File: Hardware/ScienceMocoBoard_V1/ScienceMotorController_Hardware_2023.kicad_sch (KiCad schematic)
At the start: 134 parts, among them Q1 SI4156DY, Q10 SI4156DY, Q11 SI4156DY, Q12 SI4156DY, Q13 SI4156DY, Q14 SI4156DY, Q15 SI4156DY, Q16 SI4156DY, Q2 SI4156DY, Q3 SI4156DY, Q4 SI4156DY, Q5 SI4156DY, Q6 SI4156DY, Q7 SI4156DY, Q8 SI4156DY, Q9 SI4156DY, U1 IRS2005S, U10 IRS2005S, U11 TM4C129E_Launchpad, U2 IRS2005S, U3 3V3 OKI, U4 TSR_1-2450, U5 IRS2005S, U6 IRS2005S, U7 IRS2005S, U8 IRS2005S, U9 IRS2005S

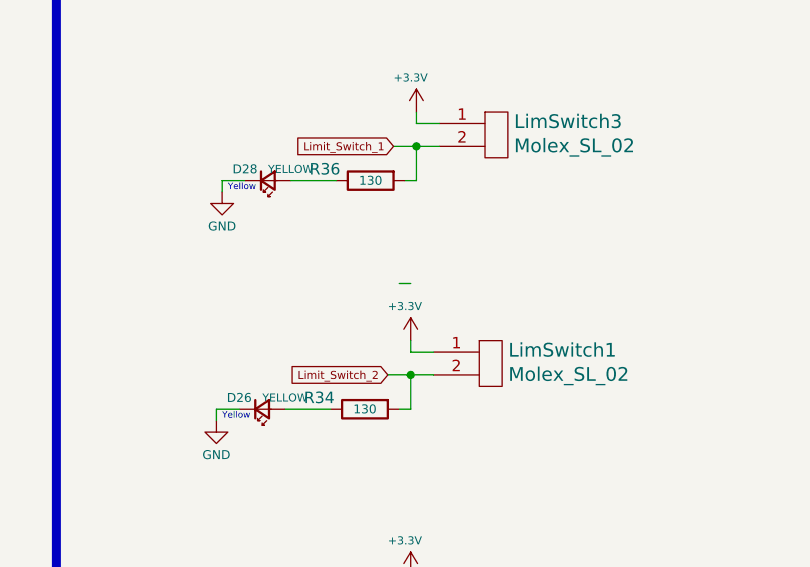
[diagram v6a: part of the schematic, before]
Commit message: Layout for Encoders, Servos, and Limit Switches
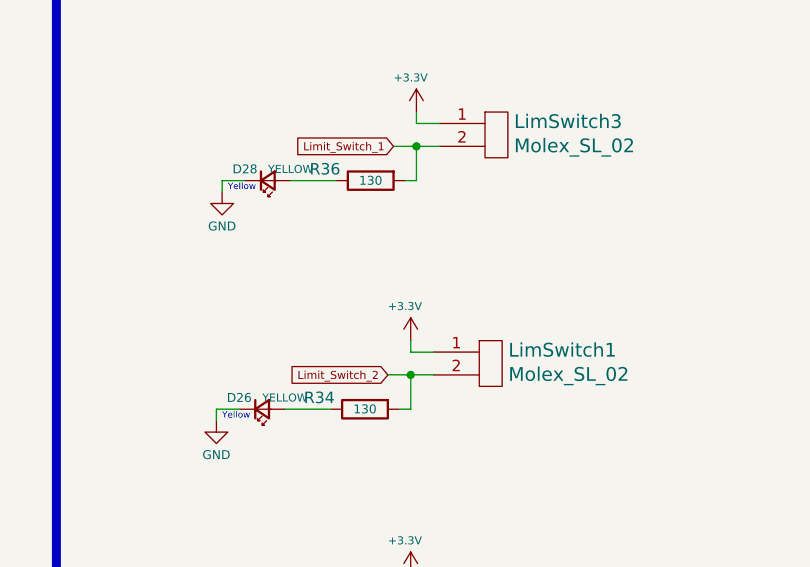
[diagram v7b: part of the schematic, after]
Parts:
- Conn1, Conn2, Conn3, Conn4, Conn5, Conn6, Conn7: footprint MRDT_Connectors:Square_Anderson_2_V_Side_By_Side -> MRDT_Connectors:Square_Anderson_2_H_Side_By_Side
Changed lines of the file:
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@@
     (stroke (width 0) (type default) (color 0 0 0 0))
   )
-  (wire (pts (xy 533.4 62.23) (xy 534.67 62.23))
-    (stroke (width 0) (type default) (color 0 0 0 0))
-  )
   (wire (pts (xy 364.49 105.41) (xy 377.19 105.41))
     (stroke (width 0) (type default) (color 0 0 0 0))
@@
       (effects (font (size 1.524 1.524)) (justify right))
     )
-    (property "Footprint" "MRDT_Connectors:Square_Anderson_2_V_Side_By_Side" (id 2) (at 52.07 330.835 0)
+    (property "Footprint" "MRDT_Connectors:Square_Anderson_2_H_Side_By_Side" (id 2) (at 52.07 330.835 0)
       (effects (font (size 1.524 1.524)) hide)
     )
@@
       (effects (font (size 1.524 1.524)) (justify right))
     )
-    (property "Footprint" "MRDT_Connectors:Square_Anderson_2_V_Side_By_Side" (id 2) (at 378.46 82.55 0)
+    (property "Footprint" "MRDT_Connectors:Square_Anderson_2_H_Side_By_Side" (id 2) (at 378.46 82.55 0)
       (effects (font (size 1.524 1.524)) hide)
     )
@@
       (effects (font (size 1.524 1.524)) (justify right))
     )
-    (property "Footprint" "MRDT_Connectors:Square_Anderson_2_V_Side_By_Side" (id 2) (at 377.825 168.91 0)
+    (property "Footprint" "MRDT_Connectors:Square_Anderson_2_H_Side_By_Side" (id 2) (at 377.825 168.91 0)
       (effects (font (size 1.524 1.524)) hide)
     )
@@
       (effects (font (size 1.524 1.524)))
     )
-    (property "Footprint" "MRDT_Connectors:Square_Anderson_2_V_Side_By_Side" (id 2) (at 139.7 201.93 0)
+    (property "Footprint" "MRDT_Connectors:Square_Anderson_2_H_Side_By_Side" (id 2) (at 139.7 201.93 0)
       (effects (font (size 1.524 1.524)) hide)
     )
@@
       (effects (font (size 1.524 1.524)) (justify right))
     )
-    (property "Footprint" "MRDT_Connectors:Square_Anderson_2_V_Side_By_Side" (id 2) (at 52.07 324.485 0)
+    (property "Footprint" "MRDT_Connectors:Square_Anderson_2_H_Side_By_Side" (id 2) (at 52.07 324.485 0)
       (effects (font (size 1.524 1.524)) hide)
     )
@@
       (effects (font (size 1.524 1.524)) (justify right))
     )
-    (property "Footprint" "MRDT_Connectors:Square_Anderson_2_V_Side_By_Side" (id 2) (at 137.16 168.91 0)
+    (property "Footprint" "MRDT_Connectors:Square_Anderson_2_H_Side_By_Side" (id 2) (at 137.16 168.91 0)
       (effects (font (size 1.524 1.524)) hide)
     )
@@
       (effects (font (size 1.524 1.524)))
     )
-    (property "Footprint" "MRDT_Connectors:Square_Anderson_2_V_Side_By_Side" (id 2) (at 380.365 201.93 0)
+    (property "Footprint" "MRDT_Connectors:Square_Anderson_2_H_Side_By_Side" (id 2) (at 380.365 201.93 0)
       (effects (font (size 1.524 1.524)) hide)
     )
@@
       (effects (font (size 1.524 1.524)) (justify right))
     )
-    (property "Footprint" "MRDT_Connectors:Square_Anderson_2_V_Side_By_Side" (id 2) (at 52.07 309.245 0)
+    (property "Footprint" "MRDT_Connectors:Square_Anderson_2_H_Side_By_Side" (id 2) (at 52.07 309.245 0)
       (effects (font (size 1.524 1.524)) hide)
     )
@@
       (effects (font (size 1.524 1.524)) (justify right))
     )
-    (property "Footprint" "MRDT_Connectors:Square_Anderson_2_V_Side_By_Side" (id 2) (at 133.35 82.55 0)
+    (property "Footprint" "MRDT_Connectors:Square_Anderson_2_H_Side_By_Side" (id 2) (at 133.35 82.55 0)
       (effects (font (size 1.524 1.524)) hide)
     )
@@
       (effects (font (size 1.524 1.524)))
     )
-    (property "Footprint" "MRDT_Connectors:Square_Anderson_2_V_Side_By_Side" (id 2) (at 27.94 321.945 0)
+    (property "Footprint" "MRDT_Connectors:Square_Anderson_2_H_Side_By_Side" (id 2) (at 27.94 321.945 0)
       (effects (font (size 1.524 1.524)) hide)
     )
@@
       (effects (font (size 1.524 1.524)) (justify right))
     )
-    (property "Footprint" "MRDT_Connectors:Square_Anderson_2_V_Side_By_Side" (id 2) (at 52.07 302.895 0)
+    (property "Footprint" "MRDT_Connectors:Square_Anderson_2_H_Side_By_Side" (id 2) (at 52.07 302.895 0)
       (effects (font (size 1.524 1.524)) hide)
     )
@@
       (effects (font (size 1.524 1.524)))
     )
-    (property "Footprint" "MRDT_Connectors:Square_Anderson_2_V_Side_By_Side" (id 2) (at 27.94 315.595 0)
+    (property "Footprint" "MRDT_Connectors:Square_Anderson_2_H_Side_By_Side" (id 2) (at 27.94 315.595 0)
       (effects (font (size 1.524 1.524)) hide)
     )
@@
       (effects (font (size 1.524 1.524)))
     )
-    (property "Footprint" "MRDT_Connectors:Square_Anderson_2_V_Side_By_Side" (id 2) (at 135.89 115.57 0)
+    (property "Footprint" "MRDT_Connectors:Square_Anderson_2_H_Side_By_Side" (id 2) (at 135.89 115.57 0)
       (effects (font (size 1.524 1.524)) hide)
     )
@@
       (effects (font (size 1.524 1.524)))
     )
-    (property "Footprint" "MRDT_Connectors:Square_Anderson_2_V_Side_By_Side" (id 2) (at 381 115.57 0)
+    (property "Footprint" "MRDT_Connectors:Square_Anderson_2_H_Side_By_Side" (id 2) (at 381 115.57 0)
       (effects (font (size 1.524 1.524)) hide)
     )
@@
     )
     (path "/b800eb0d-4e35-43a2-bf7a-748c18f9176e"
-      (reference "Conn1") (unit 1) (value "Input") (footprint "MRDT_Connectors:Square_Anderson_2_V_Side_By_Side")
+      (reference "Conn1") (unit 1) (value "Input") (footprint "MRDT_Connectors:Square_Anderson_2_H_Side_By_Side")
     )
     (path "/7ae2f7be-0b23-4959-82b9-533d8e3d95dd"
-      (reference "Conn1") (unit 2) (value "Input") (footprint "MRDT_Connectors:Square_Anderson_2_V_Side_By_Side")
+      (reference "Conn1") (unit 2) (value "Input") (footprint "MRDT_Connectors:Square_Anderson_2_H_Side_By_Side")
     )
     (path "/9c46e44a-301f-4adc-af9c-b892d007541c"
-      (reference "Conn2") (unit 1) (value "Output1") (footprint "MRDT_Connectors:Square_Anderson_2_V_Side_By_Side")
+      (reference "Conn2") (unit 1) (value "Output1") (footprint "MRDT_Connectors:Square_Anderson_2_H_Side_By_Side")
     )
     (path "/5a7c7e0b-1ab1-492d-b1f6-c5e97e39a190"
-      (reference "Conn2") (unit 2) (value "Output1") (footprint "MRDT_Connectors:Square_Anderson_2_V_Side_By_Side")
+      (reference "Conn2") (unit 2) (value "Output1") (footprint "MRDT_Connectors:Square_Anderson_2_H_Side_By_Side")
     )
     (path "/460afb3d-667d-45a6-baf1-04687f9b8568"
-      (reference "Conn3") (unit 1) (value "Output2") (footprint "MRDT_Connectors:Square_Anderson_2_V_Side_By_Side")
+      (reference "Conn3") (unit 1) (value "Output2") (footprint "MRDT_Connectors:Square_Anderson_2_H_Side_By_Side")
     )
     (path "/06cc1640-07c6-4591-9df0-cf1bc25b3c3f"
-      (reference "Conn3") (unit 2) (value "Output2") (footprint "MRDT_Connectors:Square_Anderson_2_V_Side_By_Side")
+      (reference "Conn3") (unit 2) (value "Output2") (footprint "MRDT_Connectors:Square_Anderson_2_H_Side_By_Side")
     )
     (path "/6c6e361b-4a07-4b89-a3cf-7e412883c1a4"
-      (reference "Conn4") (unit 1) (value "AndersonPP") (footprint "MRDT_Connectors:Square_Anderson_2_V_Side_By_Side")
+      (reference "Conn4") (unit 1) (value "AndersonPP") (footprint "MRDT_Connectors:Square_Anderson_2_H_Side_By_Side")
     )
     (path "/cd262ca1-3586-466d-a467-d8b01bf093a7"
-      (reference "Conn4") (unit 2) (value "AndersonPP") (footprint "MRDT_Connectors:Square_Anderson_2_V_Side_By_Side")
+      (reference "Conn4") (unit 2) (value "AndersonPP") (footprint "MRDT_Connectors:Square_Anderson_2_H_Side_By_Side")
     )
     (path "/158c6d96-163c-4c21-8189-8b32c95b4cdf"
-      (reference "Conn5") (unit 1) (value "AndersonPP") (footprint "MRDT_Connectors:Square_Anderson_2_V_Side_By_Side")
+      (reference "Conn5") (unit 1) (value "AndersonPP") (footprint "MRDT_Connectors:Square_Anderson_2_H_Side_By_Side")
     )
     (path "/de3e784e-289b-48e9-811a-b8cba0269725"
-      (reference "Conn5") (unit 2) (value "AndersonPP") (footprint "MRDT_Connectors:Square_Anderson_2_V_Side_By_Side")
+      (reference "Conn5") (unit 2) (value "AndersonPP") (footprint "MRDT_Connectors:Square_Anderson_2_H_Side_By_Side")
     )
     (path "/369feaea-9bbc-42eb-ba91-271c009547c5"
-      (reference "Conn6") (unit 1) (value "AndersonPP") (footprint "MRDT_Connectors:Square_Anderson_2_V_Side_By_Side")
+      (reference "Conn6") (unit 1) (value "AndersonPP") (footprint "MRDT_Connectors:Square_Anderson_2_H_Side_By_Side")
     )
     (path "/4f3578d9-196b-41e7-8b03-c3c988032074"
-      (reference "Conn6") (unit 2) (value "AndersonPP") (footprint "MRDT_Connectors:Square_Anderson_2_V_Side_By_Side")
+      (reference "Conn6") (unit 2) (value "AndersonPP") (footprint "MRDT_Connectors:Square_Anderson_2_H_Side_By_Side")
     )
     (path "/46f4dbf4-e603-48ae-a58c-56f6117ad989"
-      (reference "Conn7") (unit 1) (value "AndersonPP") (footprint "MRDT_Connectors:Square_Anderson_2_V_Side_By_Side")
+      (reference "Conn7") (unit 1) (value "AndersonPP") (footprint "MRDT_Connectors:Square_Anderson_2_H_Side_By_Side")
     )
     (path "/45e5d604-34a8-4ec6-8a22-709075fb152c"
-      (reference "Conn7") (unit 2) (value "AndersonPP") (footprint "MRDT_Connectors:Square_Anderson_2_V_Side_By_Side")
+      (reference "Conn7") (unit 2) (value "AndersonPP") (footprint "MRDT_Connectors:Square_Anderson_2_H_Side_By_Side")
     )
     (path "/73dc6e6e-917d-4b44-9b59-493b890a076b"
